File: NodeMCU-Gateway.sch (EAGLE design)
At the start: 28 parts, among them IC1 ATSHA204A, J2 GROVE-I2C, J3 Lipo Battery, J4 GROVE-I2C, J5 CON_HEADER_1X08-PTH, P1 PADSMALL, P2 PADNORMAL

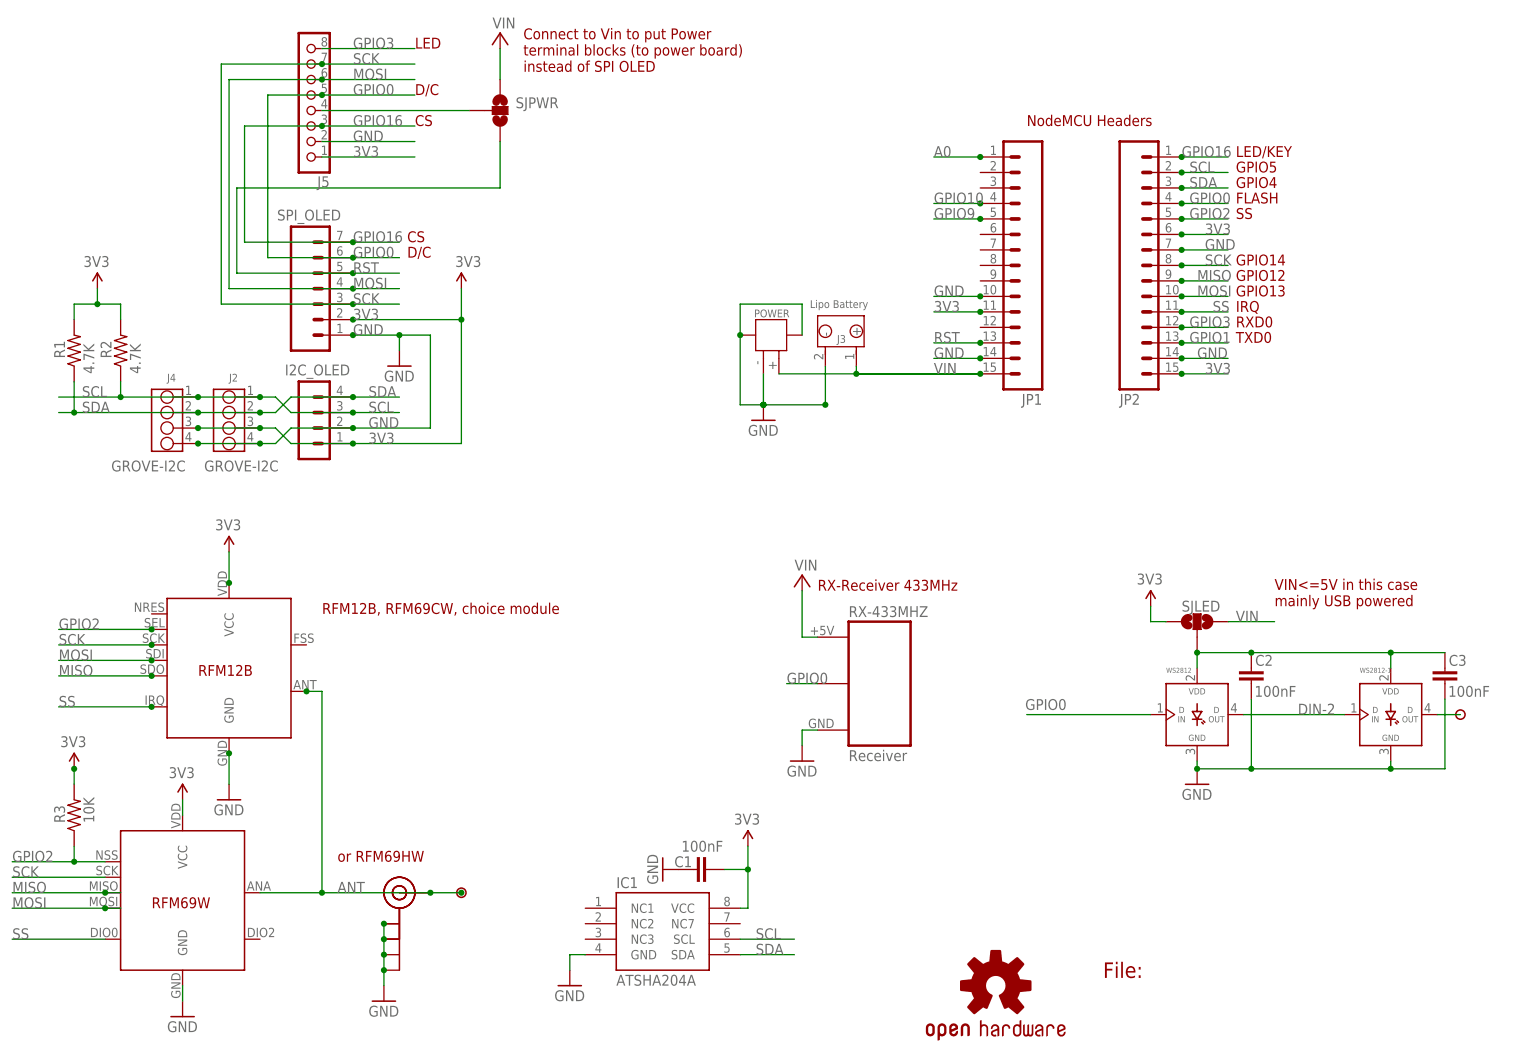
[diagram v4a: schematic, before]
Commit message: Version 1.2
Added FET to protect in case of power reverse, this avoid burning
NodeMCU board
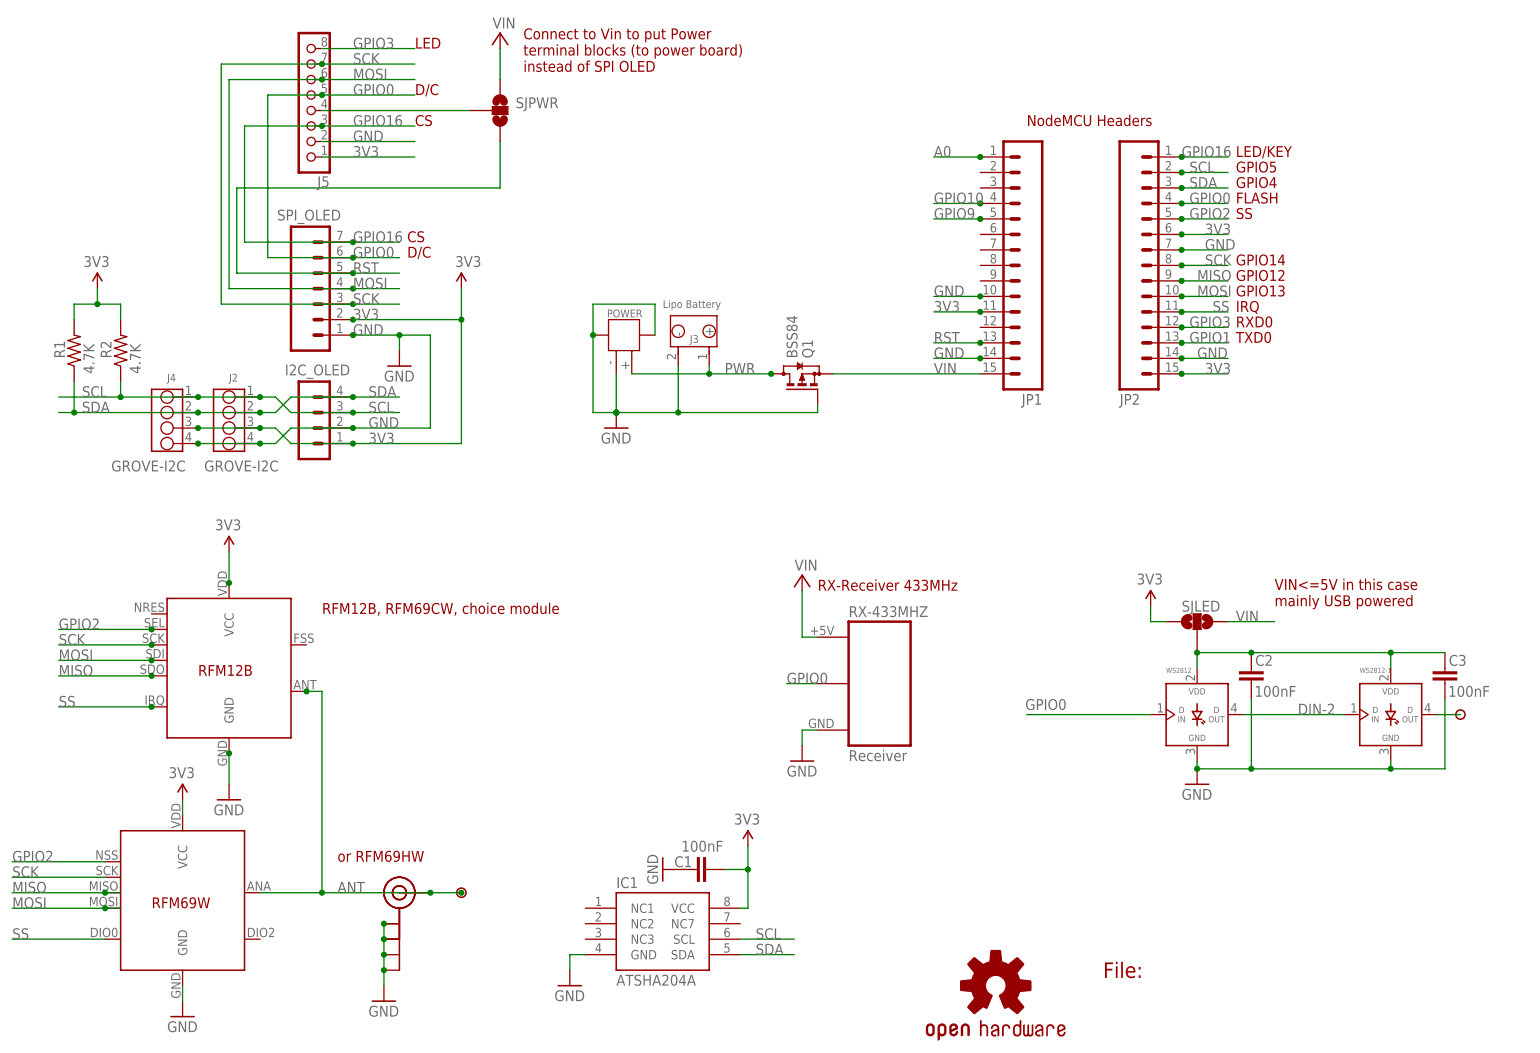
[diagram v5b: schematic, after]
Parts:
- removed R3: 10K, _c2h:RESISTOR0805-RES
- added Q1: BSS84, transistor-small-signal:BSS84
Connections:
- new net PWR: J3.+, POWER.1, Q1.D
- net 3V3: no longer R3.2
- net GND: now also Q1.G
- net GPIO2: no longer R3.1
- net VIN: now also Q1.S; no longer J3.+, POWER.1
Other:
- moved on the sheet: J3, POWER
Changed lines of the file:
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@@
 <part name="NAME" library="SparkFun-Aesthetics" deviceset="FRAME-A4L" device="" value="Value">
 <attribute name="CNAME" value="ESP8266 NodeMCU RF Gateway + Display"/>
-<attribute name="CREVISION" value="1.1a"/>
+<attribute name="CREVISION" value="1.2"/>
 <attribute name="DESIGNER" value="Charles-Henri Hallard"/>
 </part>
@@
 <part name="C3" library="_c2h" deviceset="CAP" device="0805-CAP" value="100nF"/>
 <part name="P2" library="_c2h" deviceset="PAD" device="NORMAL" value="PADNORMAL"/>
-<part name="R3" library="_c2h" deviceset="RESISTOR" device="0805-RES" value="10K"/>
-<part name="P+1" library="_c2h" deviceset="3V3-EXT" device="" value="3V3"/>
 <part name="VIN1" library="supply1" deviceset="+5V" device="" value="VIN"/>
 <part name="SJPWR" library="SparkFun-Passives" deviceset="JUMPER-PAD-3-2OF3_NC_BY_TRACE" device="_LARGE" value=""/>
@@
 <part name="GND5" library="supply1" deviceset="GND" device=""/>
 <part name="J$1" library="SparkFun-Connectors" deviceset="SMA_EDGE" device=""/>
+<part name="Q1" library="transistor-small-signal" deviceset="BSS84" device=""/>
 </parts>
 <sheets>
@@
 </plain>
 <instances>
-<instance part="GND2" gate="1" x="133.35" y="107.95"/>
+<instance part="GND2" gate="1" x="109.22" y="106.68"/>
 <instance part="GND11" gate="1" x="73.66" y="116.84"/>
 <instance part="R1" gate="G$1" x="20.32" y="119.38" smashed="yes" rot="R90">
@@
 <attribute name="VALUE" x="21.844" y="133.096" size="1.778" layer="96"/>
 </instance>
-<instance part="POWER" gate="G$1" x="134.62" y="118.11" smashed="yes" rot="R270">
-<attribute name="VALUE" x="138.43" y="120.65" size="1.27" layer="96" ratio="10" rot="R270"/>
-<attribute name="NAME" x="131.826" y="124.841" size="1.27" layer="95" ratio="10"/>
-</instance>
-<instance part="J3" gate="J" x="146.05" y="122.555" smashed="yes" rot="R270">
-<attribute name="VALUE" x="140.97" y="126.365" size="1.27" layer="96" ratio="10"/>
-<attribute name="NAME" x="145.415" y="120.65" size="1.27" layer="95" ratio="10"/>
+<instance part="POWER" gate="G$1" x="110.49" y="118.11" smashed="yes" rot="R270">
+<attribute name="VALUE" x="114.3" y="120.65" size="1.27" layer="96" ratio="10" rot="R270"/>
+<attribute name="NAME" x="107.696" y="124.841" size="1.27" layer="95" ratio="10"/>
+</instance>
+<instance part="J3" gate="J" x="121.92" y="122.555" smashed="yes" rot="R270">
+<attribute name="VALUE" x="116.84" y="126.365" size="1.27" layer="96" ratio="10"/>
+<attribute name="NAME" x="121.285" y="120.65" size="1.27" layer="95" ratio="10"/>
 </instance>
 <instance part="J4" gate="J" x="35.56" y="107.95" smashed="yes">
@@
 </instance>
 <instance part="P2" gate="G$1" x="247.65" y="59.69"/>
-<instance part="R3" gate="G$1" x="20.32" y="43.18" smashed="yes" rot="R90">
-<attribute name="NAME" x="18.8214" y="41.91" size="1.778" layer="95" rot="R90"/>
-<attribute name="VALUE" x="23.622" y="41.91" size="1.778" layer="96" rot="R90"/>
-</instance>
-<instance part="P+1" gate="3V3-EXT" x="20.32" y="50.8" smashed="yes">
-<attribute name="VALUE" x="18.034" y="54.356" size="1.778" layer="96"/>
-</instance>
 <instance part="VIN1" gate="1" x="90.17" y="171.45" smashed="yes">
 <attribute name="VALUE" x="92.71" y="173.99" size="1.778" layer="96" rot="R180"/>
@@
 <instance part="GND5" gate="1" x="116.84" y="34.29" rot="R270"/>
 <instance part="J$1" gate="1" x="73.66" y="30.48"/>
+<instance part="Q1" gate="G$1" x="139.7" y="115.57" rot="MR90"/>
 </instances>
 <busses>
@@
 <pinref part="POWER" gate="G$1" pin="3"/>
 <pinref part="GND2" gate="1" pin="GND"/>
-<wire x1="133.35" y1="110.49" x2="143.51" y2="110.49" width="0.1524" layer="91"/>
-<junction x="133.35" y="110.49"/>
-<wire x1="133.35" y1="110.49" x2="129.54" y2="110.49" width="0.1524" layer="91"/>
-<wire x1="133.35" y1="115.57" x2="133.35" y2="110.49" width="0.1524" layer="91"/>
-<wire x1="143.51" y1="116.84" x2="143.51" y2="110.49" width="0.1524" layer="91"/>
-<junction x="133.35" y="110.49"/>
-<junction x="133.35" y="110.49"/>
-<junction x="143.51" y="110.49"/>
+<wire x1="109.22" y1="109.22" x2="119.38" y2="109.22" width="0.1524" layer="91"/>
+<junction x="109.22" y="109.22"/>
+<wire x1="109.22" y1="109.22" x2="105.41" y2="109.22" width="0.1524" layer="91"/>
+<wire x1="109.22" y1="115.57" x2="109.22" y2="109.22" width="0.1524" layer="91"/>
+<wire x1="119.38" y1="116.84" x2="119.38" y2="109.22" width="0.1524" layer="91"/>
+<junction x="109.22" y="109.22"/>
+<junction x="109.22" y="109.22"/>
+<junction x="119.38" y="109.22"/>
 <pinref part="J3" gate="J" pin="-"/>
-<wire x1="139.7" y1="121.92" x2="139.7" y2="127" width="0.1524" layer="91"/>
-<wire x1="139.7" y1="127" x2="129.54" y2="127" width="0.1524" layer="91"/>
-<wire x1="129.54" y1="127" x2="129.54" y2="121.92" width="0.1524" layer="91"/>
-<junction x="129.54" y="121.92"/>
-<wire x1="129.54" y1="121.92" x2="129.54" y2="110.49" width="0.1524" layer="91"/>
+<wire x1="115.57" y1="121.92" x2="115.57" y2="127" width="0.1524" layer="91"/>
+<wire x1="115.57" y1="127" x2="105.41" y2="127" width="0.1524" layer="91"/>
+<wire x1="105.41" y1="127" x2="105.41" y2="121.92" width="0.1524" layer="91"/>
+<junction x="105.41" y="121.92"/>
+<wire x1="105.41" y1="121.92" x2="105.41" y2="109.22" width="0.1524" layer="91"/>
+<pinref part="Q1" gate="G$1" pin="G"/>
+<wire x1="119.38" y1="109.22" x2="142.24" y2="109.22" width="0.1524" layer="91"/>
+<wire x1="142.24" y1="109.22" x2="142.24" y2="110.49" width="0.1524" layer="91"/>
 </segment>
 <segment>
@@
 </segment>
 <segment>
-<pinref part="R3" gate="G$1" pin="2"/>
-<pinref part="P+1" gate="3V3-EXT" pin="3V3-EXT"/>
-<wire x1="20.32" y1="48.26" x2="20.32" y2="50.8" width="0.1524" layer="91"/>
-<junction x="20.32" y="50.8"/>
-</segment>
-<segment>
 <pinref part="P+8" gate="3V3-EXT" pin="3V3-EXT"/>
 <wire x1="130.81" y1="38.1" x2="130.81" y2="34.29" width="0.1524" layer="91"/>
@@
 <segment>
 <pinref part="U$3" gate="G$1" pin="SEL"/>
-<wire x1="25.4" y1="35.56" x2="20.32" y2="35.56" width="0.1524" layer="91"/>
 <label x="10.16" y="35.56" size="1.778" layer="95"/>
-<pinref part="R3" gate="G$1" pin="1"/>
-<wire x1="20.32" y1="35.56" x2="10.16" y2="35.56" width="0.1524" layer="91"/>
-<wire x1="20.32" y1="38.1" x2="20.32" y2="35.56" width="0.1524" layer="91"/>
-<junction x="20.32" y="35.56"/>
+<wire x1="25.4" y1="35.56" x2="10.16" y2="35.56" width="0.1524" layer="91"/>
 </segment>
 </net>
@@
 </segment>
 <segment>
-<label x="161.29" y="115.57" size="1.778" layer="95"/>
-<pinref part="JP1" gate="G$1" pin="15"/>
-<pinref part="POWER" gate="G$1" pin="1"/>
-<pinref part="J3" gate="J" pin="+"/>
-<wire x1="135.89" y1="115.57" x2="148.59" y2="115.57" width="0.1524" layer="91"/>
-<wire x1="148.59" y1="116.84" x2="148.59" y2="115.57" width="0.1524" layer="91"/>
-<junction x="148.59" y="115.57"/>
-<wire x1="168.91" y1="115.57" x2="148.59" y2="115.57" width="0.1524" layer="91"/>
-<wire x1="168.91" y1="115.57" x2="148.59" y2="115.57" width="0.1524" layer="91"/>
-<junction x="168.91" y="115.57"/>
-</segment>
-<segment>
 <wire x1="142.24" y1="72.39" x2="139.7" y2="72.39" width="0.1524" layer="91"/>
 <wire x1="139.7" y1="72.39" x2="139.7" y2="80.01" width="0.1524" layer="91"/>
@@
 <wire x1="217.17" y1="74.93" x2="209.55" y2="74.93" width="0.1524" layer="91"/>
 </segment>
+<segment>
+<pinref part="JP1" gate="G$1" pin="15"/>
+<label x="161.29" y="115.57" size="1.778" layer="95"/>
+<pinref part="Q1" gate="G$1" pin="S"/>
+<wire x1="144.78" y1="115.57" x2="168.91" y2="115.57" width="0.1524" layer="91"/>
+</segment>
 </net>
 <net name="N$2" class="0">
@@
 </segment>
 </net>
+<net name="PWR" class="0">
+<segment>
+<pinref part="POWER" gate="G$1" pin="1"/>
+<pinref part="J3" gate="J" pin="+"/>
+<wire x1="111.76" y1="115.57" x2="124.46" y2="115.57" width="0.1524" layer="91"/>
+<wire x1="124.46" y1="116.84" x2="124.46" y2="115.57" width="0.1524" layer="91"/>
+<junction x="124.46" y="115.57"/>
+<wire x1="124.46" y1="115.57" x2="134.62" y2="115.57" width="0.1524" layer="91"/>
+<label x="127" y="115.57" size="1.778" layer="95"/>
+<pinref part="Q1" gate="G$1" pin="D"/>
+<junction x="134.62" y="115.57"/>
+</segment>
+</net>

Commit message: Bump to V1.3
* SMA/UFL Antenna connector has been size reduced
* Antenna trace and RF Module surrounded with via for better RF
isolation
* I2C OLED connector is now "lock" version, you can just plug to test it
will fit without connector
* No more LED solder pad to choose VIN/3V3, added 1N4148 diode from 5V
for the 1st LED to decrease VCC to 4.4V, always works
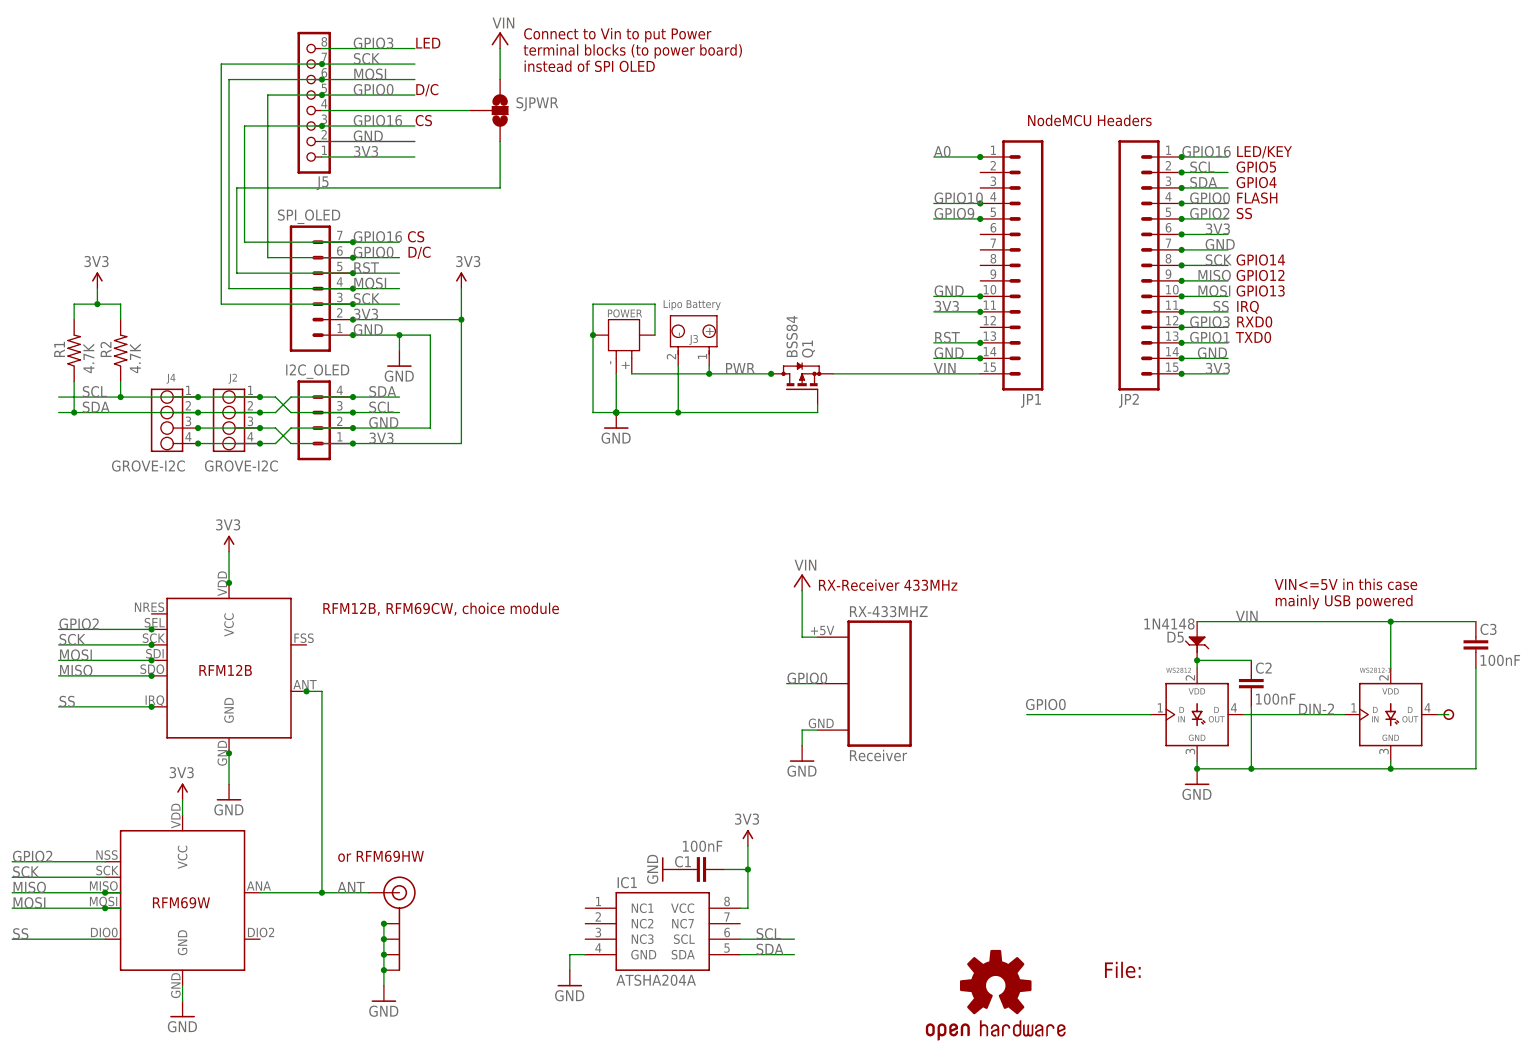
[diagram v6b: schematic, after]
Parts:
- removed J$1: SMA_EDGE, SparkFun-Connectors:SMA_EDGE
- removed P1: PADSMALL, SteveMarple:PADSMALL
- removed SJLED: JUMPER-PAD-3-2OF3_NC_BY_TRACE_LARGE, SparkFun-Passives:JUMPER-PAD-3-2OF3_NC_BY_TRACE_LARGE
- removed U-FL: U.FL, microbuilder:U.FL
- added D5: 1N4148, Seeed-Discrete:D-ESD-2P-CESD5V0D1
- added J$2: ANTENNATINY, _c2h:ANTENNATINY
- I2C_OLED: value CON_HEADER_1X04'SMALL'' -> CON_HEADER_1X04'LOCK'; device _c2h:CON_HEADER_1X04'SMALL'' -> _c2h:CON_HEADER_1X04'LOCK'
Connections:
- removed net VLED: C2.2, C3.2, SJLED.2, WS2812-1.VDD, WS2812.VDD
- new net N$3: C2.2, D5.2, WS2812.VDD
- net 3V3: no longer SJLED.3
- net ANT: now also J$2.SIGNAL; no longer J$1.SIGNAL, P1.1, U-FL.SIGNAL
- net GND: now also J$2.GND@0, J$2.GND@1, J$2.GND@2, J$2.GND@3; no longer J$1.GND@0, J$1.GND@1, J$1.GND@2, J$1.GND@3, U-FL.GND@0, U-FL.GND@1
- net VIN: now also C3.2, D5.1, WS2812-1.VDD; no longer SJLED.1
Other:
- moved on the sheet: C2, C3
